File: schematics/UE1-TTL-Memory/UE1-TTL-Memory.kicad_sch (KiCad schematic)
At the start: 6 parts, among them J1 Edge 1, J2 Edge 2

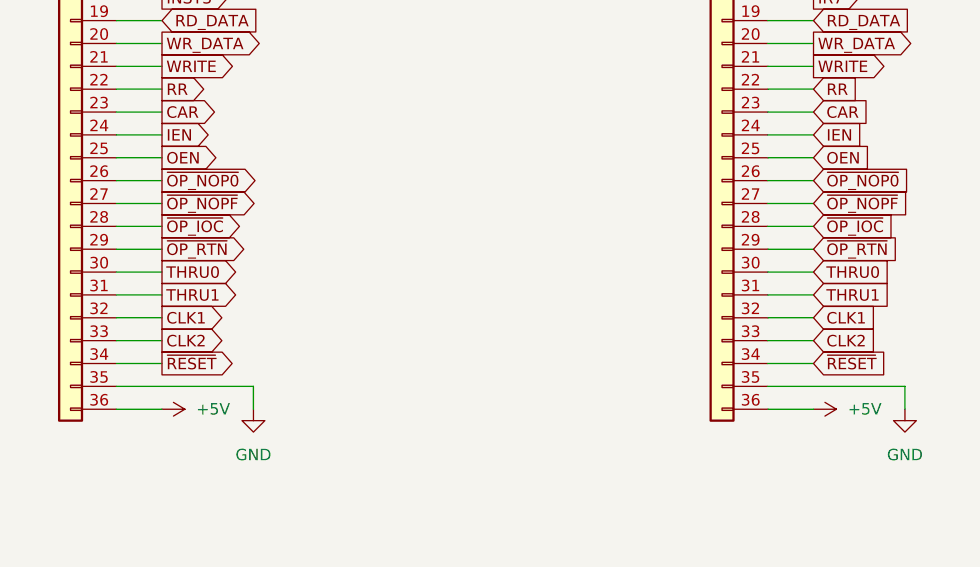
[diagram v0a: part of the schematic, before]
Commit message: Add a tape "REWIND" opcode to reset the PC early
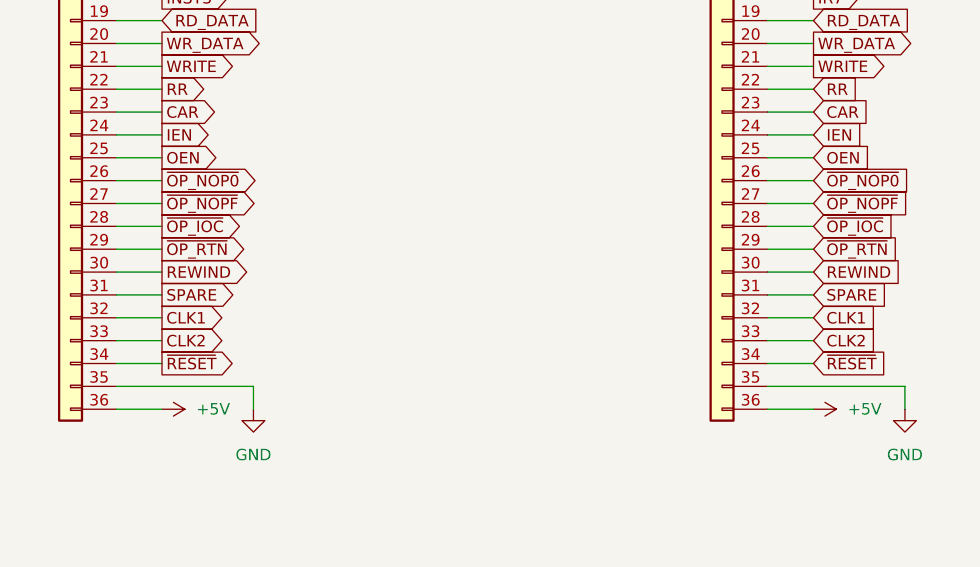
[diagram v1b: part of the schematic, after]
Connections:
- net THRU0 renamed REWIND
- net THRU1 renamed SPARE
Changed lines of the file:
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@@
 		)
 	)
-	(global_label "THRU0"
+	(global_label "REWIND"
 		(shape output)
 		(at 109.22 139.7 0)
@@
 		)
 		(property "Intersheetrefs" "${INTERSHEET_REFS}"
-			(at 118.3133 139.7 0)
+			(at 119.2809 139.7 0)
 			(effects
 				(font
@@
 		)
 	)
-	(global_label "THRU1"
+	(global_label "SPARE"
 		(shape output)
 		(at 109.22 142.24 0)
@@
 		)
 		(property "Intersheetrefs" "${INTERSHEET_REFS}"
-			(at 118.3133 142.24 0)
+			(at 118.1923 142.24 0)
 			(effects
 				(font
@@
 		)
 	)
-	(global_label "THRU1"
+	(global_label "SPARE"
 		(shape input)
 		(at 181.61 142.24 0)
@@
 		)
 		(property "Intersheetrefs" "${INTERSHEET_REFS}"
-			(at 190.7033 142.24 0)
+			(at 190.5823 142.24 0)
 			(effects
 				(font
@@
 		)
 	)
-	(global_label "THRU0"
+	(global_label "REWIND"
 		(shape input)
 		(at 181.61 139.7 0)
@@
 		)
 		(property "Intersheetrefs" "${INTERSHEET_REFS}"
-			(at 190.7033 139.7 0)
-			(effects
-				(font
+			(at 191.6709 139.7 0)
+			(effects
+				(font

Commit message: Lay out memory board
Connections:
- net INST0: no longer names the net of J1.15 (Pin_15)
- net INST1: no longer names the net of J1.16 (Pin_16)
- net INST2: no longer names the net of J1.17 (Pin_17)
- net INST3: no longer names the net of J1.18 (Pin_18)
- no-connect marks 1 -> 5
